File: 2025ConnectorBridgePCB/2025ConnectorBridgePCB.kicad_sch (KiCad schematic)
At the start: 9 parts, among them J1 DA15_Socket, J2 DA15_Socket, J3 Conn_01x03_Socket, J4 Conn_01x05_Socket, J5 Conn_01x03_Socket, J6 Conn_01x05_Socket, J7 Conn_01x03_Socket, P1 USB_C_Plug_USB2.0, U1 MCP2551-I-SN

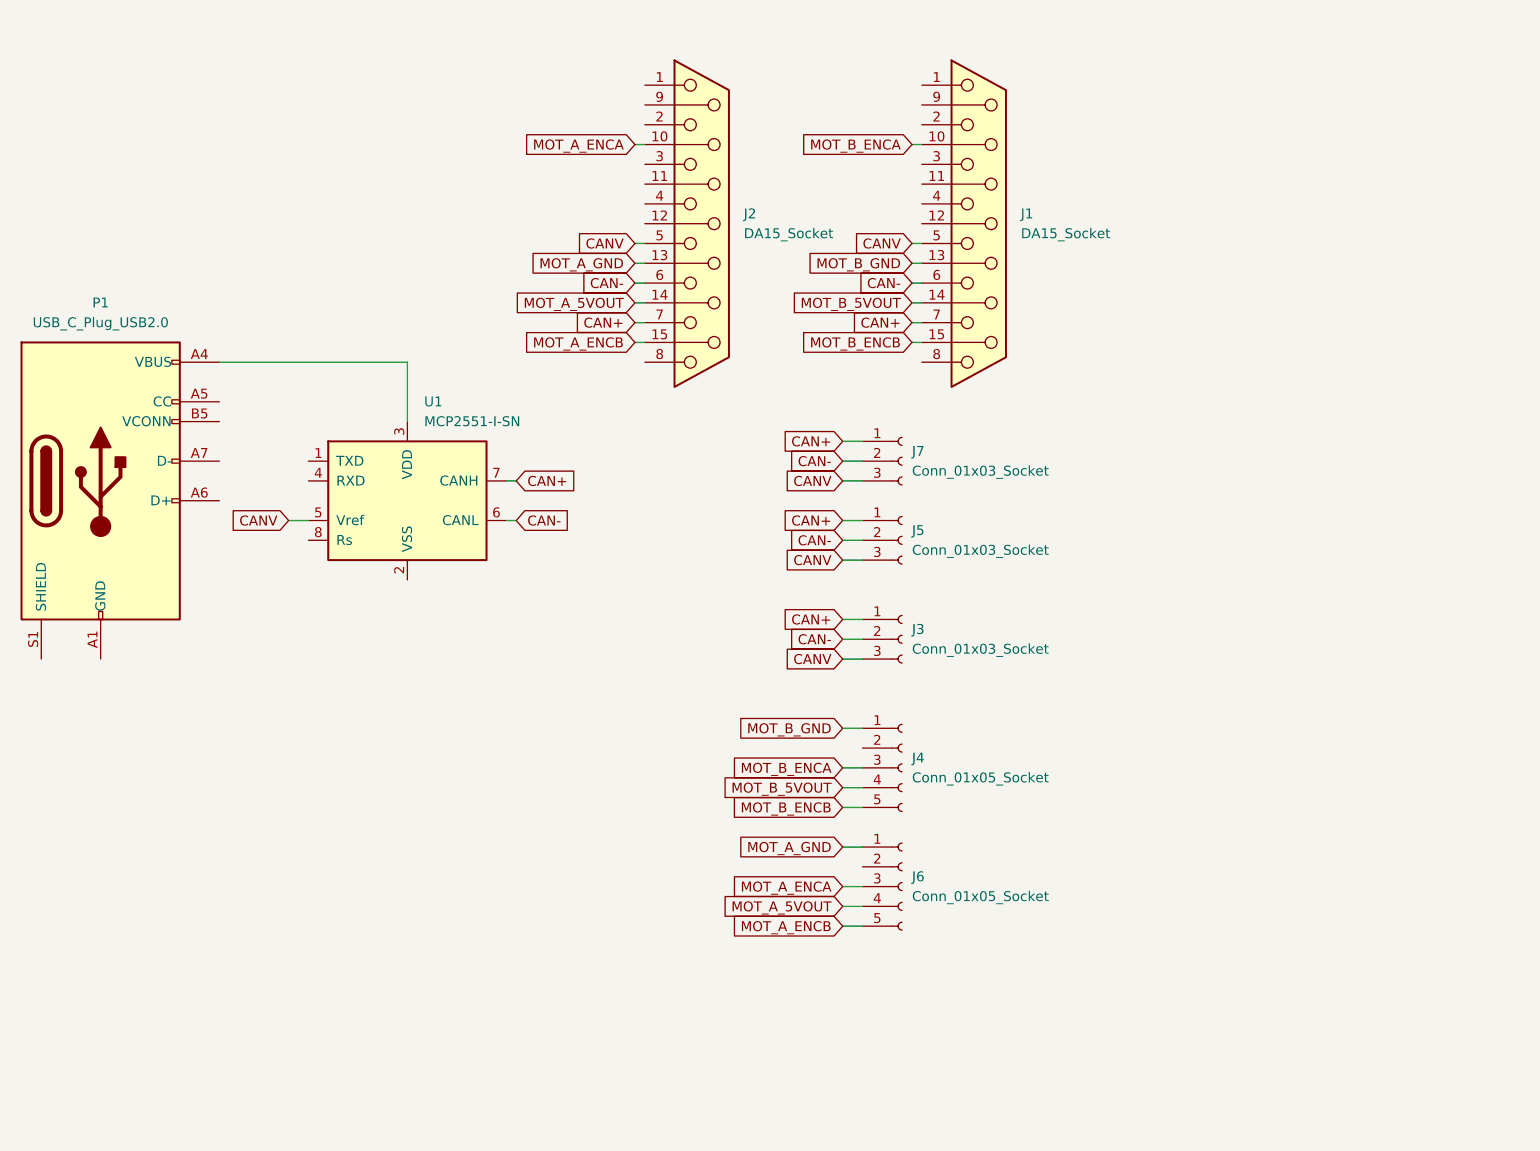
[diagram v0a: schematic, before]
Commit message: Replace USB/MCP2515 with daughter board thru hole idea
We were discussing at one point soldering on a daughter board  that houses USB CAN functionality. We can make a branch for onboard USB-CAN functionality
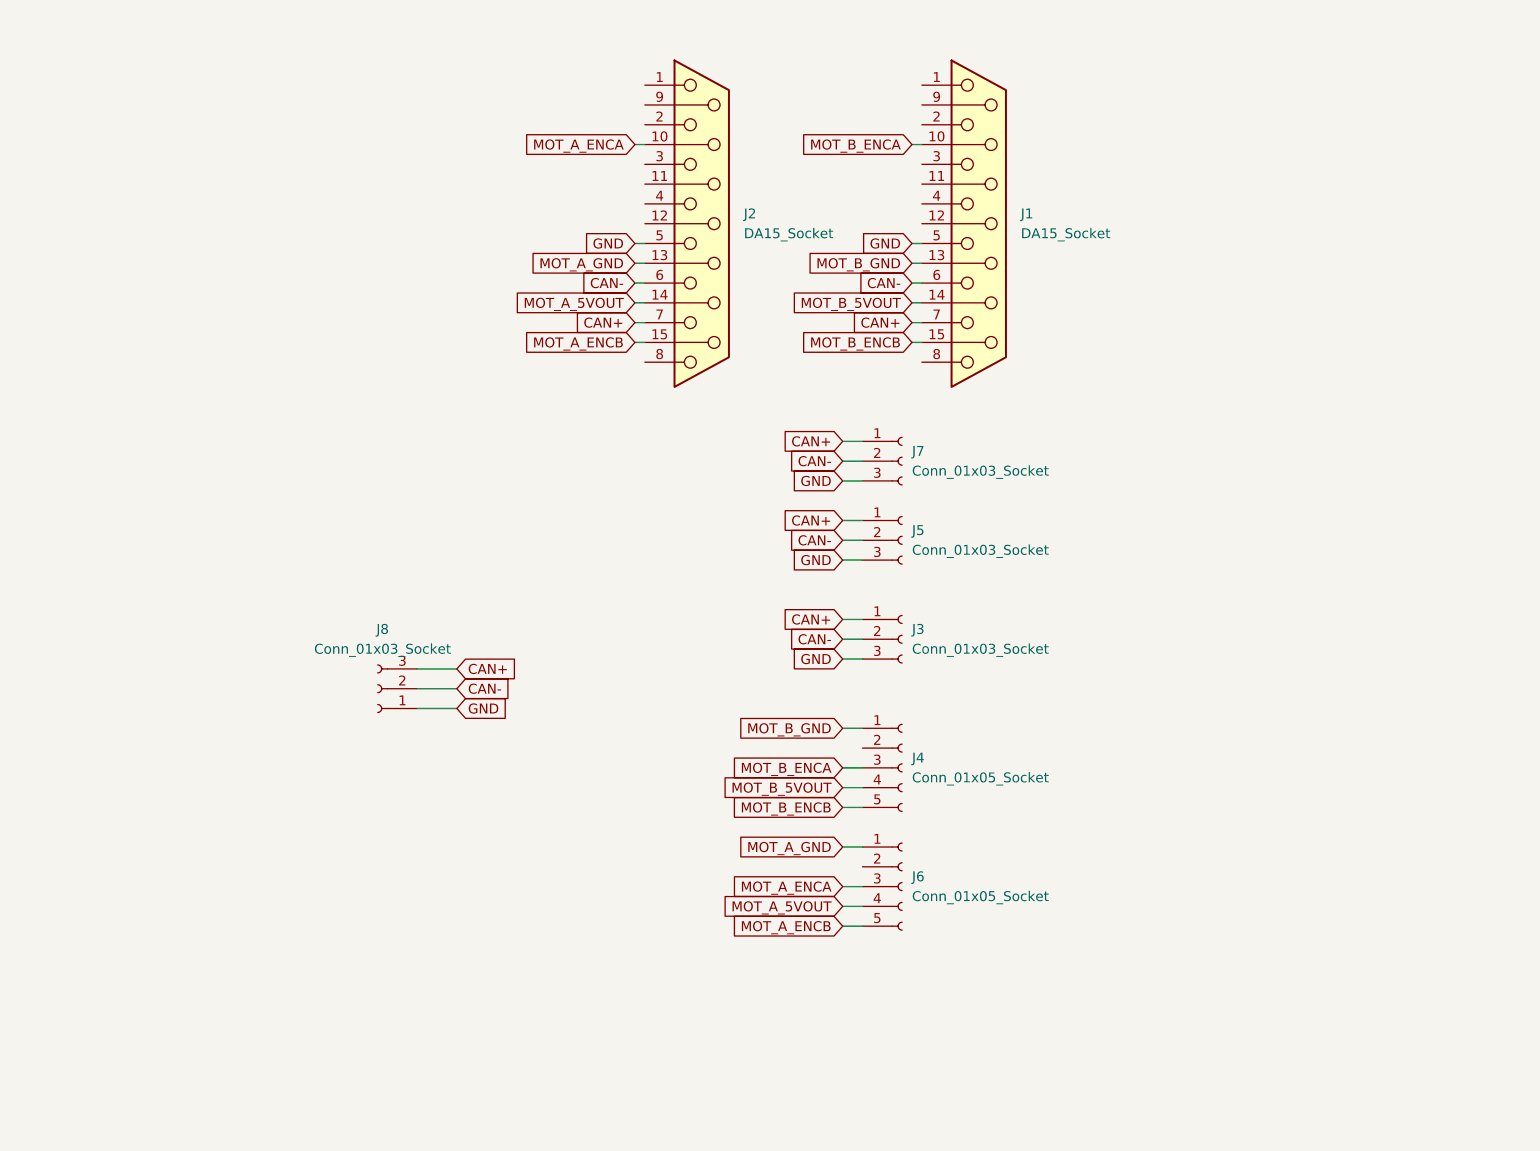
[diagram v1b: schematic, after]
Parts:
- removed P1: USB_C_Plug_USB2.0, Connector_USB:USB_C_Plug_JAE_DX07P024AJ1, symbol Connector:USB_C_Plug_USB2.0
- removed U1: MCP2551-I-SN, Package_SO:SOIC-8_3.9x4.9mm_P1.27mm, symbol Interface_CAN_LIN:MCP2551-I-SN
- added J8: Conn_01x03_Socket, Connector_Wire:SolderWire-0.25sqmm_1x03_P4.2mm_D0.65mm_OD1.7mm, symbol Connector:Conn_01x03_Socket
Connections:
- net CAN+: now also J8.3 (Pin_3)
- net CAN-: now also J8.2 (Pin_2)
- net CANV renamed GND
- net GND: now also J8.1 (Pin_1)

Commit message: Shrink Everything, Use proper Encoder Connectors
This also adds a screw terminal, not wired up yet but it will breakout unused pins from DB15.
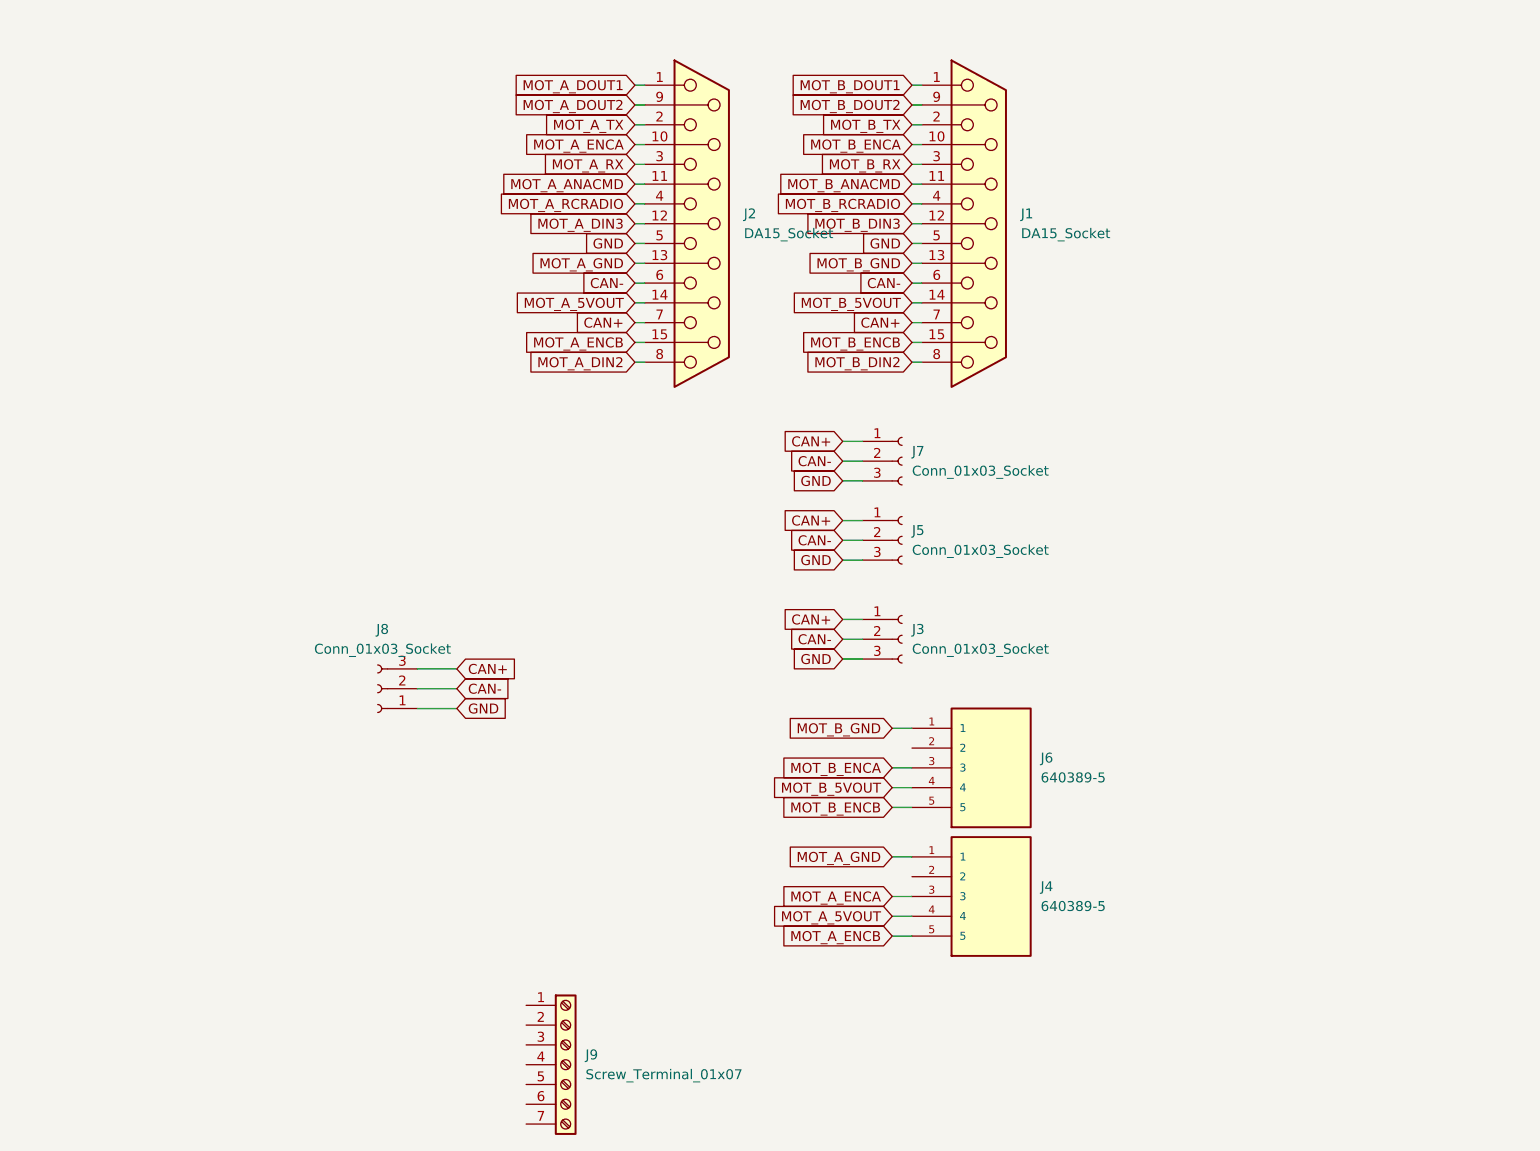
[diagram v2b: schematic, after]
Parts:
- removed J4, J6: Conn_01x05_Socket, Connector_TE-Connectivity:TE_826576-5_1x05_P3.96mm_Vertical, symbol Connector:Conn_01x05_Socket
- added J4, J6: 640389-5, 640389-5:TE_640389-5, symbol 640389-5:640389-5
- added J9: Screw_Terminal_01x07, TerminalBlock_Phoenix:TerminalBlock_Phoenix_MKDS-1,5-7-5.08_1x07_P5.08mm_Horizontal, symbol Connector:Screw_Terminal_01x07
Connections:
- net MOT_A_5VOUT: now also J4.4
- net MOT_A_ENCA: now also J4.3
- net MOT_A_ENCB: now also J4.5
- net MOT_A_GND: now also J4.1
- net MOT_B_5VOUT: now also J6.4
- net MOT_B_ENCA: now also J6.3
- net MOT_B_ENCB: now also J6.5
- net MOT_B_GND: now also J6.1
- net MOT_A_DOUT1: now reaches J2.1
- net MOT_A_ANACMD: now reaches J2.11 (P111)
- net MOT_A_DIN3: now reaches J2.12 (P12)
- net MOT_A_TX: now reaches J2.2
- net MOT_A_RX: now reaches J2.3
- net MOT_A_RCRADIO: now reaches J2.4
- net MOT_A_DIN2: now reaches J2.8
- net MOT_A_DOUT2: now reaches J2.9 (P9)
- net MOT_B_DOUT1: now reaches J1.1
- net MOT_B_ANACMD: now reaches J1.11 (P111)
- net MOT_B_DIN3: now reaches J1.12 (P12)
- net MOT_B_TX: now reaches J1.2
- net MOT_B_RX: now reaches J1.3
- net MOT_B_RCRADIO: now reaches J1.4
- net MOT_B_DIN2: now reaches J1.8
- net MOT_B_DOUT2: now reaches J1.9 (P9)

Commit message: Proper connectors
Use proper connectors for CAN, Encoders, and DB-15. Breakout unused DB-15 pads to screw terminals.
Also added mounting holes but did not fillet corners yet in case dimensions need to be changed.
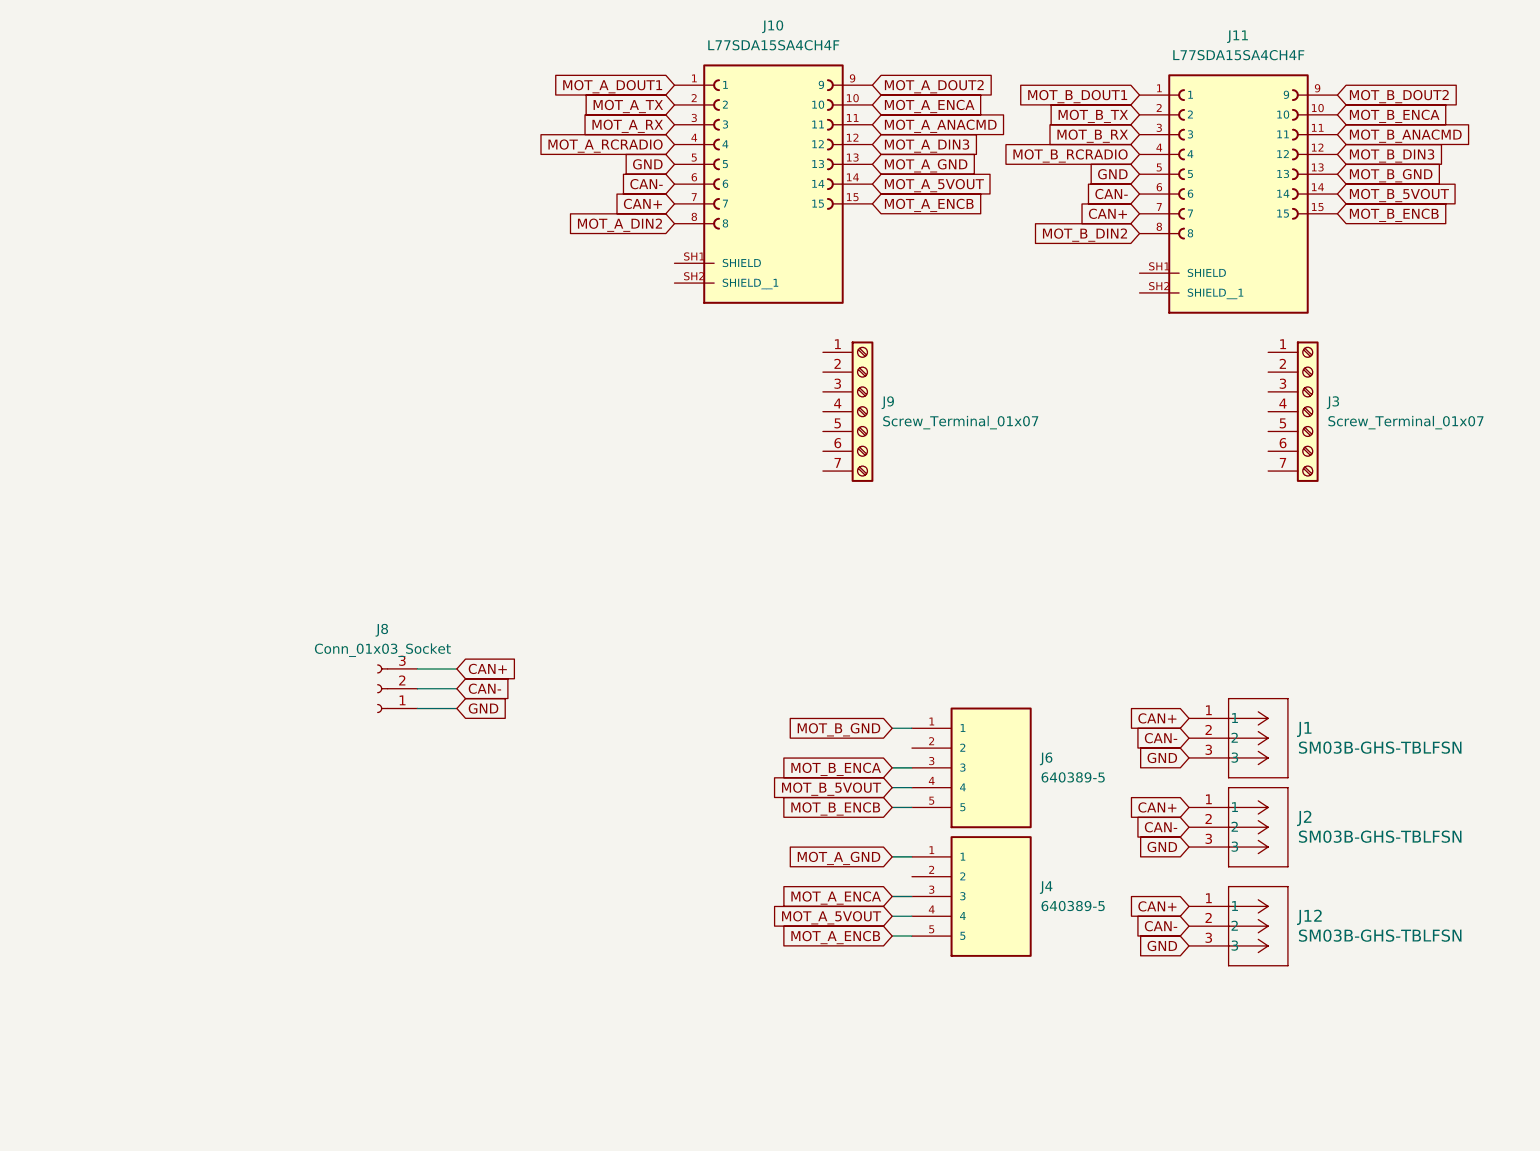
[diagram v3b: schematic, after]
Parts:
- removed J1, J2: DA15_Socket, Connector_Dsub:DSUB-15_Socket_Horizontal_P2.77x2.54mm_EdgePinOffset9.40mm, symbol Connector:DA15_Socket
- removed J3, J5, J7: Conn_01x03_Socket, Connector_JST:JST_ZE_S03B-ZESK-2D_1x03_P1.50mm_Horizontal, symbol Connector:Conn_01x03_Socket
- added J1, J12, J2: SM03B-GHS-TBLFSN, SM03B_GHS_TB_LF__SN_:CONN_SM03B-GHS-TBLFSN_JST, symbol 2026-02-04_00-19-45:SM03B-GHS-TBLFSN
- added J10, J11: L77SDA15SA4CH4F, L77SDA15SA4CH4F:AMPHENOL_L77SDA15SA4CH4F, symbol L77SDA15SA4CH4F:L77SDA15SA4CH4F
- added J3: Screw_Terminal_01x07, TerminalBlock_Phoenix:TerminalBlock_Phoenix_MKDS-1,5-7-5.08_1x07_P5.08mm_Horizontal, symbol Connector:Screw_Terminal_01x07
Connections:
- net CAN+: now also J1.1, J10.7, J11.7, J12.1, J2.1
- net CAN-: now also J1.2, J10.6, J11.6, J12.2, J2.2
- net GND: now also J1.3, J10.5, J11.5, J12.3, J2.3
- net MOT_A_5VOUT: now also J10.14
- net MOT_A_ANACMD: now also J10.11
- net MOT_A_DIN2: now also J10.8
- net MOT_A_DIN3: now also J10.12
- net MOT_A_DOUT1: now also J10.1
- net MOT_A_DOUT2: now also J10.9
- net MOT_A_ENCA: now also J10.10
- net MOT_A_ENCB: now also J10.15
- net MOT_A_GND: now also J10.13
- net MOT_A_RCRADIO: now also J10.4
- net MOT_A_RX: now also J10.3
- net MOT_A_TX: now also J10.2
- net MOT_B_5VOUT: now also J11.14
- net MOT_B_ANACMD: now also J11.11
- net MOT_B_DIN2: now also J11.8
- net MOT_B_DIN3: now also J11.12
- net MOT_B_DOUT1: now also J11.1
- net MOT_B_DOUT2: now also J11.9
- net MOT_B_ENCA: now also J11.10
- net MOT_B_ENCB: now also J11.15
- net MOT_B_GND: now also J11.13
- net MOT_B_RCRADIO: now also J11.4
- net MOT_B_RX: now also J11.3
- net MOT_B_TX: now also J11.2
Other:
- moved on the sheet: J9

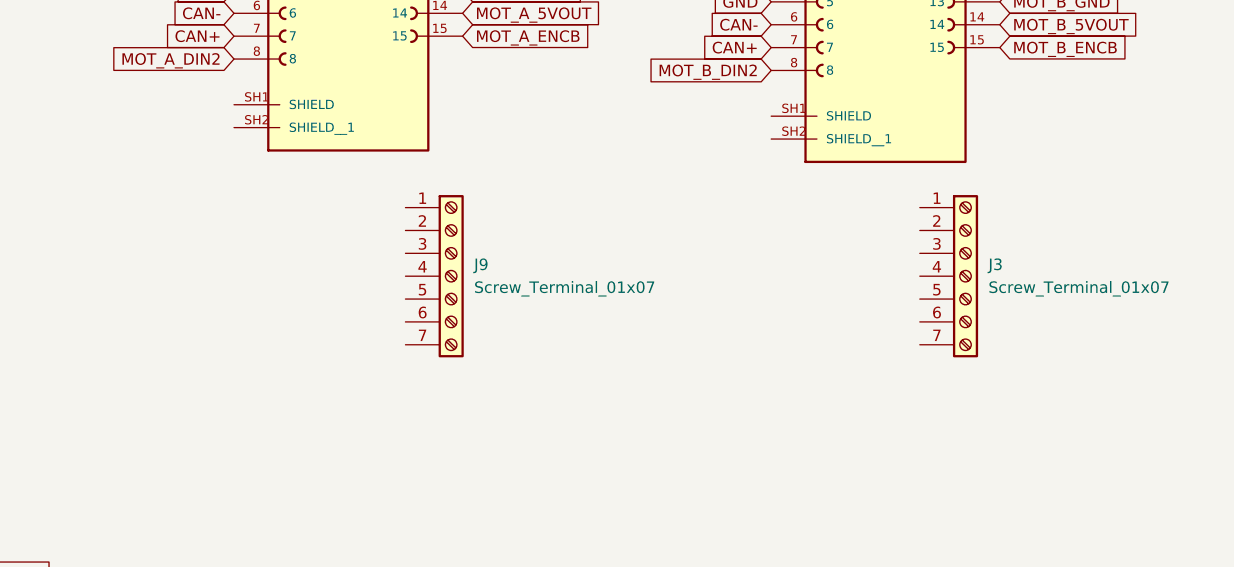
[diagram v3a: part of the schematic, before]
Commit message: Comm Board: Push Latest Changes
Moved text back onto board, updated some traces.
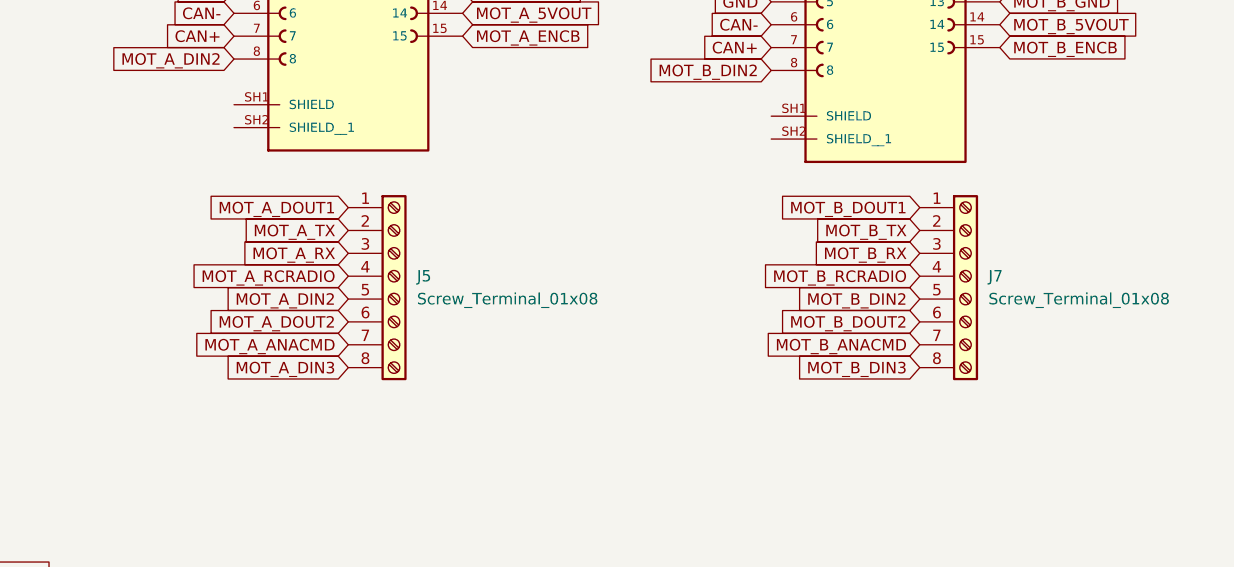
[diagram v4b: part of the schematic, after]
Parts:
- removed J3, J9: Screw_Terminal_01x07, TerminalBlock_Phoenix:TerminalBlock_Phoenix_MKDS-1,5-7-5.08_1x07_P5.08mm_Horizontal, symbol Connector:Screw_Terminal_01x07
- added J5, J7: Screw_Terminal_01x08, TerminalBlock_Phoenix:TerminalBlock_Phoenix_MKDS-1,5-8_1x08_P5.00mm_Horizontal, symbol Connector:Screw_Terminal_01x08
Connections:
- net MOT_A_ANACMD: now also J5.7 (Pin_7)
- net MOT_A_DIN2: now also J5.5 (Pin_5)
- net MOT_A_DIN3: now also J5.8 (Pin_8)
- net MOT_A_DOUT1: now also J5.1 (Pin_1)
- net MOT_A_DOUT2: now also J5.6 (Pin_6)
- net MOT_A_RCRADIO: now also J5.4 (Pin_4)
- net MOT_A_RX: now also J5.3 (Pin_3)
- net MOT_A_TX: now also J5.2 (Pin_2)
- net MOT_B_ANACMD: now also J7.7 (Pin_7)
- net MOT_B_DIN2: now also J7.5 (Pin_5)
- net MOT_B_DIN3: now also J7.8 (Pin_8)
- net MOT_B_DOUT1: now also J7.1 (Pin_1)
- net MOT_B_DOUT2: now also J7.6 (Pin_6)
- net MOT_B_RCRADIO: now also J7.4 (Pin_4)
- net MOT_B_RX: now also J7.3 (Pin_3)
- net MOT_B_TX: now also J7.2 (Pin_2)
